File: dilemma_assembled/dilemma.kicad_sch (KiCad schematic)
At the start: 105 parts, among them J1 USB_C_Receptacle_USB2.0, J102 NA_serial, J105 Conn_01x04_Female, J113 Cirque, J2 Conn_01x03_Female, J5 Conn_01x02, SW1 SW_Push, SW101 NA_SW_Push, SW102 NA_SW_Push, SW103 NA_SW_Push, SW104 NA_SW_Push, SW105 NA_SW_Push, SW106 NA_SW_Push, SW107 NA_SW_Push, SW108 NA_SW_Push, SW109 NA_SW_Push, SW110 NA_SW_SPST, SW112 NA_SW_Push, SW113 NA_SW_Push, SW114 NA_SW_Push, SW115 NA_SW_Push, SW116 NA_SW_Push, SW117 NA_SW_Push, SW118 NA_SW_Push, SW119 NA_SW_Push, SW2 SW_Push, SW3001 NA_SW_Push, SW3002 RotaryEncoder_Switch, U1 RP2040, U2 GD25Q80CEIGR, U3 XC6210B332MR-G, U4 USBLC6-2P6, Y1 Crystal_GND24

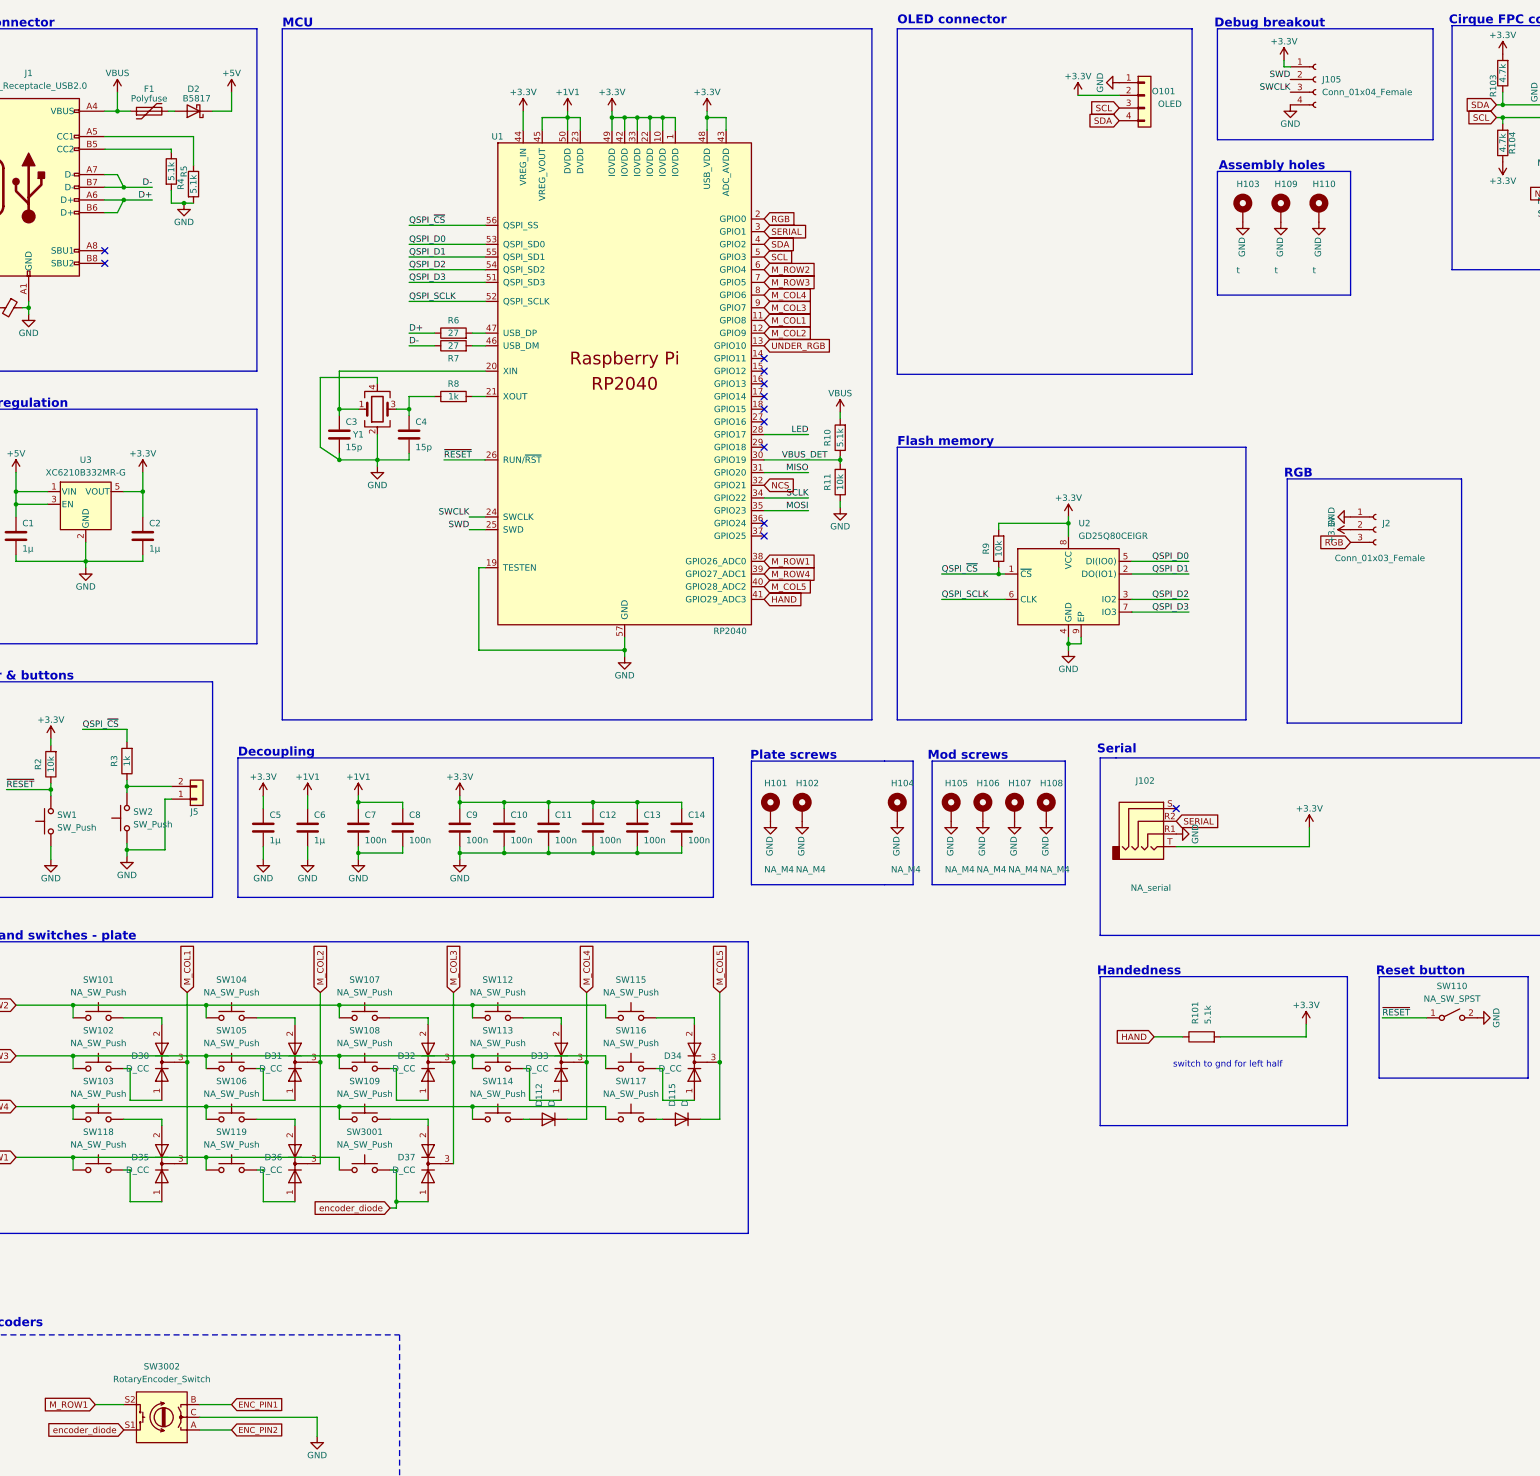
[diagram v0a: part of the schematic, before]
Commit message: routing, non assembled components
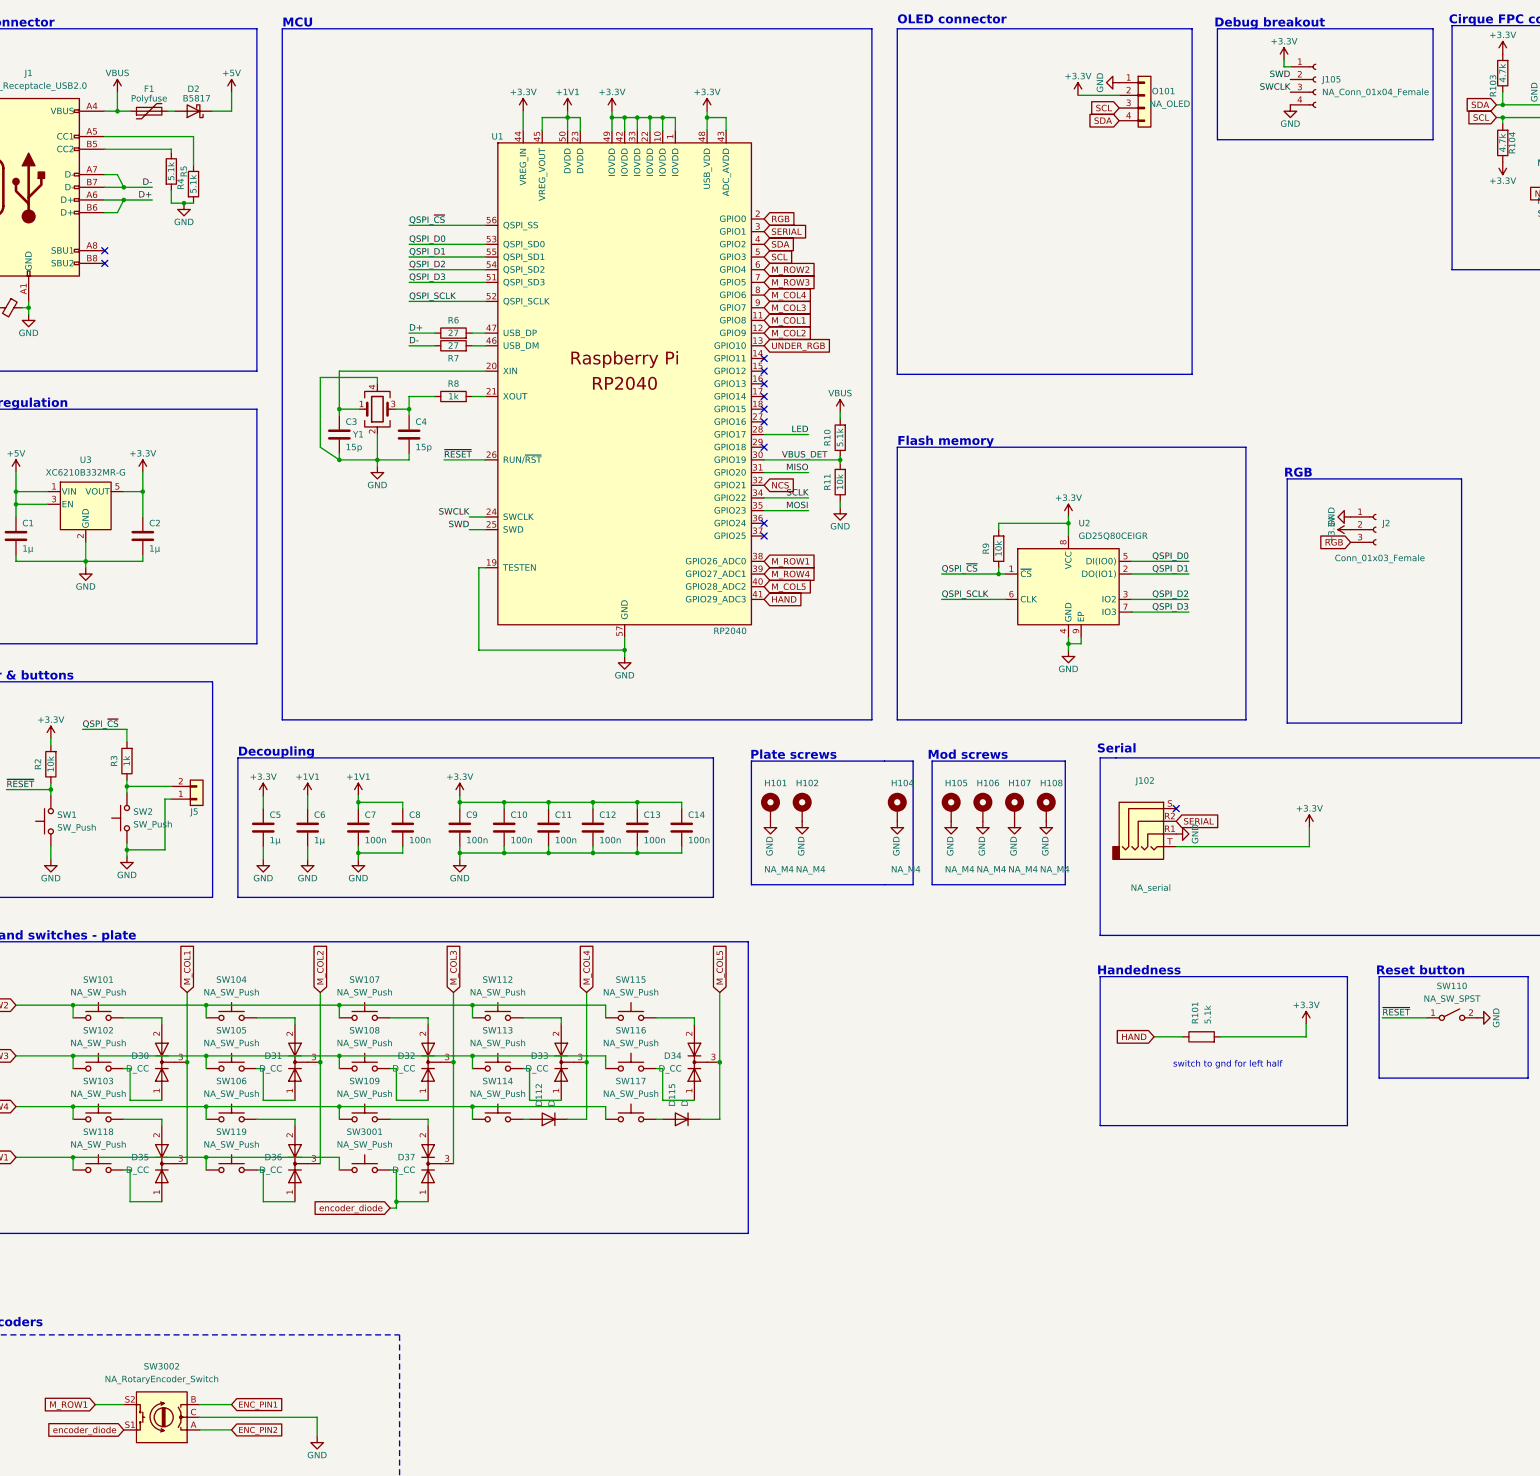
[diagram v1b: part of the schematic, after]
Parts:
- removed H103, H109, H110: t, local-libraries:JLC_SMT_Assembly_Hole, symbol Mechanical:MountingHole_Pad
- J105: value Conn_01x04_Female -> NA_Conn_01x04_Female
- O101: value OLED -> NA_OLED
- SW3002: value RotaryEncoder_Switch -> NA_RotaryEncoder_Switch
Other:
- note removed: "Assembly holes"

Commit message: cleanup
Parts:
- J2: value Conn_01x03_Female -> NA_Conn_01x03_Female
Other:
- note added: "reverse for left half"
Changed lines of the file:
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@@
     (effects (font (size 1.778 1.778) (thickness 0.3556) bold) (justify left bottom))
   )
+  (text "reverse for left half" (at 288.925 191.77 0)
+    (effects (font (size 1.27 1.27)) (justify left bottom))
+  )
   (text "Flash memory" (at 209.55 104.14 0)
     (effects (font (size 1.778 1.778) (thickness 0.3556) bold) (justify left bottom))
@@
       (effects (font (size 1.27 1.27)) (justify left))
     )
-    (property "Value" "Conn_01x03_Female" (id 1) (at 297.18 126.365 0)
+    (property "Value" "NA_Conn_01x03_Female" (id 1) (at 297.18 126.365 0)
       (effects (font (size 1.27 1.27)) (justify left))
     )
@@
     )
     (path "/c5d656d9-c5c5-43f3-9bd2-fbf74bcf52f9"
-      (reference "J2") (unit 1) (value "Conn_01x03_Female") (footprint "local-libraries:PinHeader_1x03_P2.54mm_Vertical_smd")
+      (reference "J2") (unit 1) (value "NA_Conn_01x03_Female") (footprint "local-libraries:PinHeader_1x03_P2.54mm_Vertical_smd")
     )
     (path "/06b6e523-10ae-4799-8871-3c7a3a700ad9"

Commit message: change flash memory
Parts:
- removed U2: GD25Q80CEIGR, 0xLib_Package_DFN_QFN:USON-8-1EP_3x2mm_P0.5mm_EP0.25x1.65mm, symbol Memory_Flash:W25Q32JVZP
- added J?: GC9A01, prettylib:GC9A01-biggers hole, symbol kbd:IPS_LCD__gc9a01_240X240
- added U2: W25Q128JVS, drawings:W25Q128JVPIQ, symbol Memory_Flash:W25Q128JVS
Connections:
- net +3V3: now also U2.8 (VCC)
- net GND: now also J?.2 (GND), U2.4 (GND)
- net MOSI: now also J?.4 (MOSI)
- net QSPI_D0: now also U2.5 (DI(IO0))
- net QSPI_D1: now also U2.2 (DO(IO1))
- net QSPI_D2: now also U2.3 (IO2)
- net QSPI_D3: now also U2.7 (IO3)
- net QSPI_SCLK: now also U2.6 (CLK)
- net QSPI_~{CS}: now also U2.1 (~{CS})
- new net LCD_PWR: J?.1 (VCC)
- new net QP_CS: J?.6 (~{CS})
- new net QP_DC: J?.5 (D/C)
- new net QP_RST: J?.7 (RST)
- new net SCK: J?.3 (SCK)
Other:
- note added: "LCD"
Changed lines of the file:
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@@
     (stroke (width 0) (type default) (color 0 0 0 0))
   )
+  (polyline (pts (xy 417.195 123.825) (xy 417.195 172.72))
+    (stroke (width 0) (type default) (color 0 0 0 0))
+  )
   (wire (pts (xy 71.12 226.06) (xy 97.79 226.06))
     (stroke (width 0) (type default) (color 0 0 0 0))
@@
     (stroke (width 0) (type default) (color 0 0 0 0))
   )
+  (wire (pts (xy 396.24 132.08) (xy 398.78 132.08))
+    (stroke (width 0) (type default) (color 0 0 0 0))
+  )
   (wire (pts (xy 64.135 44.45) (xy 64.135 45.085))
     (stroke (width 0) (type default) (color 0 0 0 0))
@@
     (stroke (width 0) (type default) (color 0 0 0 0))
   )
+  (polyline (pts (xy 382.27 123.825) (xy 382.27 172.72))
+    (stroke (width 0) (type default) (color 0 0 0 0))
+  )
   (wire (pts (xy 97.79 88.9) (xy 127 88.9))
     (stroke (width 0) (type default) (color 0 0 0 0))
@@
     (stroke (width 0) (type default) (color 0 0 0 0))
   )
+  (polyline (pts (xy 417.195 172.72) (xy 382.27 172.72))
+    (stroke (width 0) (type default) (color 0 0 0 0))
+  )
   (wire (pts (xy 123.825 120.65) (xy 127 120.65))
     (stroke (width 0) (type default) (color 0 0 0 0))
@@
     (stroke (width 0) (type default) (color 0 0 0 0))
   )
+  (polyline (pts (xy 382.27 123.825) (xy 417.195 123.825))
+    (stroke (width 0) (type default) (color 0 0 0 0))
+  )
   (wire (pts (xy 54.61 113.03) (xy 58.42 113.03))
     (stroke (width 0) (type default) (color 0 0 0 0))
@@
     (effects (font (size 1.778 1.778) (thickness 0.3556) bold) (justify right bottom))
   )
+  (text "LCD" (at 381.635 123.825 0)
+    (effects (font (size 1.778 1.778) (thickness 0.3556) bold) (justify left bottom))
+  )
   (text "Cirque FPC connector" (at 320.04 19.685 0)
     (effects (font (size 1.778 1.778) (thickness 0.3556) bold) (justify left bottom))
@@
     )
   )
+  (global_label "SCK" (shape input) (at 396.24 137.16 0) (fields_autoplaced)
+    (effects (font (size 1.27 1.27)) (justify left))
+    (property "Intersheet References" "${INTERSHEET_REFS}" (id 0) (at 402.4026 137.0806 0)
+      (effects (font (size 1.27 1.27)) (justify left) hide)
+    )
+  )
   (global_label "M_ROW3" (shape input) (at 33.02 226.06 180)
     (effects (font (size 1.27 1.27)) (justify right))
@@
     )
   )
+  (global_label "QP_RST" (shape input) (at 396.24 147.32 0) (fields_autoplaced)
+    (effects (font (size 1.27 1.27)) (justify left))
+    (property "Intersheet References" "${INTERSHEET_REFS}" (id 0) (at 405.6683 147.2406 0)
+      (effects (font (size 1.27 1.27)) (justify left) hide)
+    )
+  )
   (global_label "SDA" (shape input) (at 329.565 35.56 180)
     (effects (font (size 1.27 1.27)) (justify right))
@@
     )
   )
+  (global_label "QP_DC" (shape input) (at 396.24 142.24 0) (fields_autoplaced)
+    (effects (font (size 1.27 1.27)) (justify left))
+    (property "Intersheet References" "${INTERSHEET_REFS}" (id 0) (at 404.7612 142.1606 0)
+      (effects (font (size 1.27 1.27)) (justify left) hide)
+    )
+  )
   (global_label "M_ROW1" (shape input) (at 182.88 127 0)
     (effects (font (size 1.27 1.27)) (justify left))
@@
     )
   )
+  (global_label "LCD_PWR" (shape output) (at 398.78 132.08 0) (fields_autoplaced)
+    (effects (font (size 1.27 1.27)) (justify left))
+    (property "Intersheet References" "${INTERSHEET_REFS}" (id 0) (at 129.54 -330.2 0)
+      (effects (font (size 1.27 1.27)) hide)
+    )
+  )
   (global_label "RGB" (shape input) (at 182.88 58.42 0)
     (effects (font (size 1.27 1.27)) (justify left))
@@
     )
   )
+  (global_label "QP_CS" (shape input) (at 396.24 144.78 0) (fields_autoplaced)
+    (effects (font (size 1.27 1.27)) (justify left))
+    (property "Intersheet References" "${INTERSHEET_REFS}" (id 0) (at 404.7007 144.7006 0)
+      (effects (font (size 1.27 1.27)) (justify left) hide)
+    )
+  )
+  (global_label "MOSI" (shape input) (at 396.24 139.7 0) (fields_autoplaced)
+    (effects (font (size 1.27 1.27)) (justify left))
+    (property "Intersheet References" "${INTERSHEET_REFS}" (id 0) (at 403.2493 139.6206 0)
+      (effects (font (size 1.27 1.27)) (justify left) hide)
+    )
+  )
   (global_label "NCS" (shape input) (at 342.265 53.34 180)
     (effects (font (size 1.27 1.27)) (justify right))
@@
     (pin "2")
   )
-  (symbol (lib_id "Memory_Flash:W25Q32JVZP") (at 243.84 132.08 0) (unit 1)
-    (in_bom yes) (on_board yes) (fields_autoplaced)
-    (property "Reference" "U2" (id 0) (at 245.8594 119.38 0)
-      (effects (font (size 1.27 1.27)) (justify left))
-    )
-    (property "Value" "GD25Q80CEIGR" (id 1) (at 245.8594 121.92 0)
-      (effects (font (size 1.27 1.27)) (justify left))
-    )
-    (property "Footprint" "0xLib_Package_DFN_QFN:USON-8-1EP_3x2mm_P0.5mm_EP0.25x1.65mm" (id 2) (at 243.84 132.08 0)
-      (effects (font (size 1.27 1.27)) hide)
-    )
-    (property "Datasheet" "" (id 3) (at 243.84 132.08 0)
-      (effects (font (size 1.27 1.27)) hide)
-    )
-    (property "LCSC" "C395484" (id 4) (at 243.84 132.08 0)
-      (effects (font (size 1.27 1.27)) hide)
-    )
-    (pin "1")
-    (pin "2")
-    (pin "3")
-    (pin "4")
-    (pin "5")
-    (pin "6")
-    (pin "7")
-    (pin "8")
-    (pin "9")
-  )
   (symbol (lib_id "Device:D_Dual_CommonCathode_AAK") (at 88.9 247.65 90) (unit 1)
     (in_bom yes) (on_board yes) (fields_autoplaced)
@@
     (pin "1")
   )
+  (symbol (lib_id "kbd:IPS_LCD__gc9a01_240X240") (at 392.43 139.7 0) (mirror y) (unit 1)
+    (in_bom no) (on_board yes)
+    (property "Reference" "J?" (id 0) (at 389.636 127 0)
+      (effects (font (size 1.27 1.27)) (justify left))
+    )
+    (property "Value" "GC9A01" (id 1) (at 391.922 128.778 0)
+      (effects (font (size 1.27 1.27)) (justify left))
+    )
+    (property "Footprint" "prettylib:GC9A01-biggers hole" (id 2) (at 391.16 124.46 0)
+      (effects (font (size 1.27 1.27)) hide)
+    )
+    (property "Datasheet" "~" (id 3) (at 391.16 124.46 0)
+      (effects (font (size 1.27 1.27)) hide)
+    )
+    (pin "1")
+    (pin "2")
+    (pin "3")
+    (pin "4")
+    (pin "5")
+    (pin "6")
+    (pin "7")
+  )
   (symbol (lib_id "Device:C") (at 91.44 180.34 0) (unit 1)
     (in_bom yes) (on_board yes)
@@
     (pin "9")
   )
+  (symbol (lib_id "Memory_Flash:W25Q128JVS") (at 243.84 132.08 0) (unit 1)
+    (in_bom yes) (on_board yes) (fields_autoplaced)
+    (property "Reference" "U2" (id 0) (at 245.8594 119.38 0)
+      (effects (font (size 1.27 1.27)) (justify left))
+    )
+    (property "Value" "W25Q128JVS" (id 1) (at 245.8594 121.92 0)
+      (effects (font (size 1.27 1.27)) (justify left))
+    )
+    (property "Footprint" "drawings:W25Q128JVPIQ" (id 2) (at 243.84 132.08 0)
+      (effects (font (size 1.27 1.27)) hide)
+    )
+    (property "Datasheet" "http://www.winbond.com/resource-files/w25q128jv_dtr%20revc%2003272018%20plus.pdf" (id 3) (at 243.84 132.08 0)
+      (effects (font (size 1.27 1.27)) hide)
+    )
+    (pin "1")
+    (pin "2")
+    (pin "3")
+    (pin "4")
+    (pin "5")
+    (pin "6")
+    (pin "7")
+    (pin "8")
+  )
   (symbol (lib_id "Mechanical:MountingHole_Pad") (at 220.345 176.53 0) (unit 1)
     (in_bom yes) (on_board yes)
@@
     (pin "1")
   )
+  (symbol (lib_id "power:GND") (at 396.24 134.62 90) (unit 1)
+    (in_bom yes) (on_board yes)
+    (property "Reference" "#PWR?" (id 0) (at 402.59 134.62 0)
+      (effects (font (size 1.27 1.27)) hide)
+    )
+    (property "Value" "GND" (id 1) (at 400.6342 134.493 0))
+    (property "Footprint" "" (id 2) (at 396.24 134.62 0)
+      (effects (font (size 1.27 1.27)) hide)
+    )
+    (property "Datasheet" "" (id 3) (at 396.24 134.62 0)
+      (effects (font (size 1.27 1.27)) hide)
+    )
+    (pin "1")
+  )
   (symbol (lib_id "Device:C") (at 130.81 180.34 0) (unit 1)
     (in_bom yes) (on_board yes)
@@
       (reference "#PWR0132") (unit 1) (value "+3.3V") (footprint "")
     )
+    (path "/f1f8c5e8-84ec-46cc-976a-c595f2716600"
+      (reference "#PWR?") (unit 1) (value "GND") (footprint "")
+    )
     (path "/4a21e78b-0ab0-4b88-8132-9b174e045719"
       (reference "C1") (unit 1) (value "1µ") (footprint "Capacitor_SMD:C_0603_1608Metric")
@@
       (reference "J113") (unit 1) (value "Cirque") (footprint "local-libraries:FPC-SMD_FPC05012-09200-.5mm")
     )
+    (path "/6e2411cd-fd67-4be2-b1a3-b3e54de4894a"
+      (reference "J?") (unit 1) (value "GC9A01") (footprint "prettylib:GC9A01-biggers hole")
+    )
     (path "/66096f4f-c798-4425-8537-e7adeb21bec3"
       (reference "O101") (unit 1) (value "NA_OLED") (footprint "local-libraries:PinHeader_1x04_P2.54mm_Vertical")
@@
       (reference "U1") (unit 1) (value "RP2040") (footprint "0xLib_Package_DFN_QFN:QFN-56-1EP_7x7mm_P0.4mm_EP3.2x3.2mm")
     )
-    (path "/3b628cb4-77fa-40d4-8aa3-0ae0b973ec32"
-      (reference "U2") (unit 1) (value "GD25Q80CEIGR") (footprint "0xLib_Package_DFN_QFN:USON-8-1EP_3x2mm_P0.5mm_EP0.25x1.65mm")
+    (path "/f05b539d-f3ed-4d87-8562-322d3113dab5"
+      (reference "U2") (unit 1) (value "W25Q128JVS") (footprint "drawings:W25Q128JVPIQ")
     )
     (path "/33208a57-5054-4bad-b85f-35da7b25e7bb"
